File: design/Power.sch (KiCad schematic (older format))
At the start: 49 parts, among them U2 NCP1117ST33T3G, U3 DRV8302

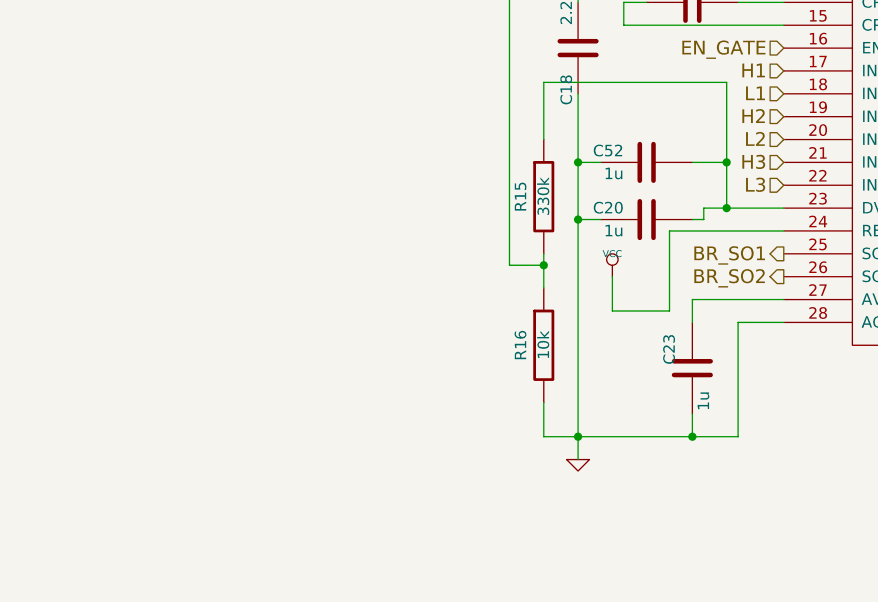
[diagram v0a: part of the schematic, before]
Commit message: Changed some capacitor values, made new assembly PDFs, added comment about R16 to schematic
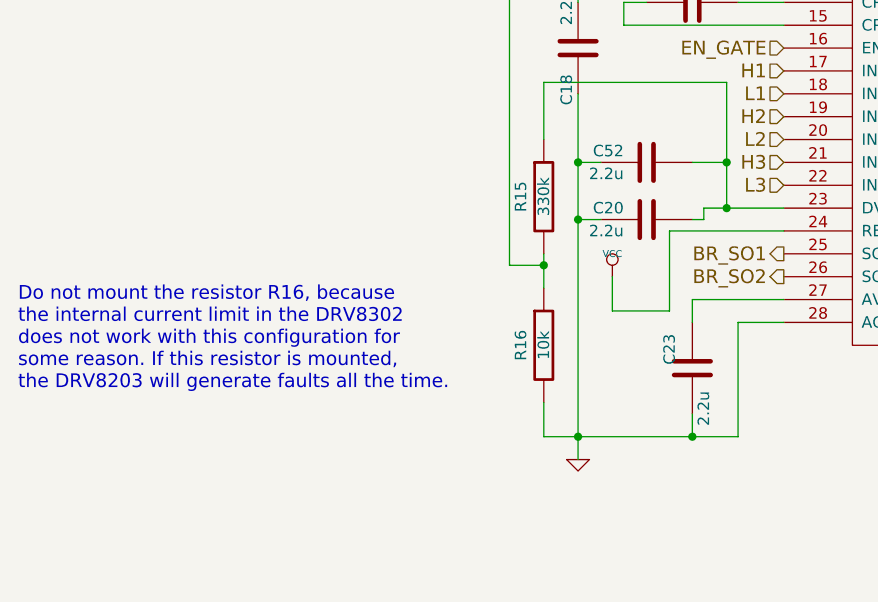
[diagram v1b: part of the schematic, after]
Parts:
- C20, C23, C52: value 1u -> 2.2u
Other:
- note added: "Do not mount the resistor R16, because\nthe internal current limit in the DRV8302\ndoes not work with this configuration for\nsome reason. If this resistor is mounted, \nthe DRV8203 will generate faults all the time."
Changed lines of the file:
@@
 P 3950 4800
 F 0 "C20" V 4000 4900 50  0000 L CNN
-F 1 "1u" V 3900 4900 50  0000 L CNN
+F 1 "2.2u" V 3900 4900 50  0000 L CNN
 F 2 "SMD_Packages:SMD-0603_c" H 3950 4800 60  0001 C CNN
 F 3 "" H 3950 4800 60  0001 C CNN
@@
 P 4150 5450
 F 0 "C23" V 4250 5300 50  0000 L CNN
-F 1 "1u" V 4100 5550 50  0000 L CNN
+F 1 "2.2u" V 4100 5550 50  0000 L CNN
 F 2 "SMD_Packages:SMD-0805" H 4150 5450 60  0001 C CNN
 F 3 "" H 4150 5450 60  0001 C CNN
@@
 P 3950 4550
 F 0 "C52" V 4000 4650 50  0000 L CNN
-F 1 "1u" V 3900 4650 50  0000 L CNN
+F 1 "2.2u" V 3900 4650 50  0000 L CNN
 F 2 "SMD_Packages:SMD-0603_c" H 3950 4550 60  0001 C CNN
 F 3 "" H 3950 4550 60  0001 C CNN
@@
 0D 0D 85 50 5B 08 A1 71 E3 C6 45 47 47 77 AB F8 CD C0 F0 65 C3 18 9A 0F 4F 4B 4B 4B 51 51 51 53
 53 93 40 20 30 31 31 61 94 40 19 18 18 43 C3 C0 C0 A0 72 FE 07 CF 64 8C 61 E1 12 74 DD 00 00 00
-00 49 45 4E 44 AE 42 60 82 CF
+00 49 45 4E 44 AE 42 60 82 05
 EndData
 $EndBitmap
@@
 20 10 88 31 C3 77 F3 62 81 40 20 10 08 04 02 81 E0 1F 14 E4 21 10 08 04 02 81 40 8C 41 50 90 87
 40 20 10 08 04 02 31 06 41 41 1E 02 81 40 20 10 08 C4 18 E4 FF 01 14 B1 03 90 4A B9 68 69 00 00
-00 00 49 45 4E 44 AE 42 60 82 03
+00 00 49 45 4E 44 AE 42 60 82 00
 EndData
 $EndBitmap
@@
 A1 C7 18 00 00 C0 28 C8 B2 00 00 00 46 41 96 05 00 00 30 0A B2 2C 00 00 80 51 90 65 01 00 00 8C
 82 2C 0B 00 00 60 14 64 59 00 00 00 A3 FC 7F BD 9B 69 A6 C1 67 F0 EA 00 00 00 00 49 45 4E 44 AE
-42 60 82 0F
+42 60 82 5F
 EndData
 $EndBitmap
@@
 AB D8 39 0B 59 91 9E DF A8 2A 5B EE 54 3A FD 71 ED 71 2F 29 C3 82 EC 80 87 06 6E C3 98 10 30 3B
 62 9A BB 2D 03 B8 C4 64 FC B5 26 AC 13 9B D1 39 40 41 C1 D6 78 4C 84 BF 94 F0 6F E1 BF 96 F0 0F
-FF 77 E2 FF 1F 0F 43 55 32 21 1C 08 16 00 00 00 00 49 45 4E 44 AE 42 60 82 79
+FF 77 E2 FF 1F 0F 43 55 32 21 1C 08 16 00 00 00 00 49 45 4E 44 AE 42 60 82 4E
 EndData
 $EndBitmap
+Text Notes 1200 5550 0    60   ~ 0
+Do not mount the resistor R16, because\nthe internal current limit in the DRV8302\ndoes not work with this configuration for\nsome reason. If this resistor is mounted, \nthe DRV8203 will generate faults all the time.
 $EndSCHEMATC

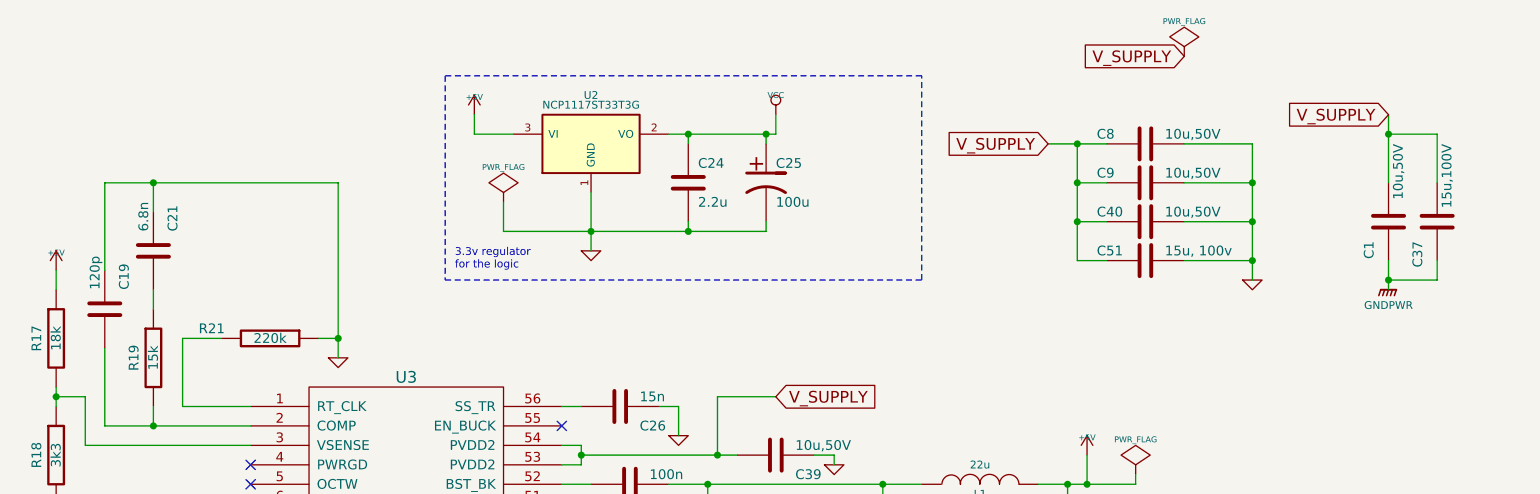
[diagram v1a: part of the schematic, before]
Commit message: Added TVS diode, moved some traces
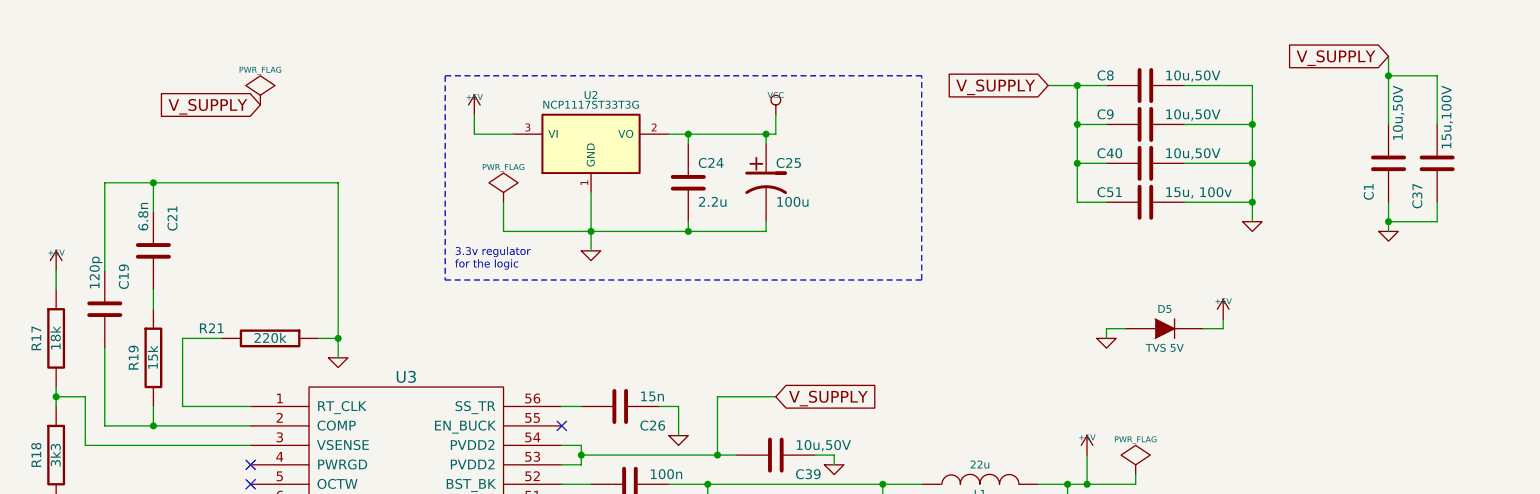
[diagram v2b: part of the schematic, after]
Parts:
- added D5: TVS 5V, w_smd_diode:do214ac, symbol DIODE
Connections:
- net GNDPWR is gone; now on net GND: C1.1, C37.1
- net +5V: now also D5.2 (K)
- net GND: now also D5.1 (A)
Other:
- moved on the sheet: C1, C37, C40, C51, C8, C9
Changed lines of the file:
@@
 LIBS:crf_1
 LIBS:BLDC_4-cache
-EELAYER 25 0
+EELAYER 24 0
 EELAYER END
 $Descr A4 11693 8268
@@
 L PWR_FLAG #FLG066
 U 1 1 505105A5
-P 9350 750
-F 0 "#FLG066" H 9350 845 30  0001 C CNN
-F 1 "PWR_FLAG" H 9350 930 30  0000 C CNN
-F 2 "" H 9350 750 60  0001 C CNN
-F 3 "" H 9350 750 60  0001 C CNN
-	1    9350 750
+P 4600 1000
+F 0 "#FLG066" H 4600 1095 30  0001 C CNN
+F 1 "PWR_FLAG" H 4600 1180 30  0000 C CNN
+F 2 "" H 4600 1000 60  0001 C CNN
+F 3 "" H 4600 1000 60  0001 C CNN
+	1    4600 1000
 	1    0    0    -1
 $EndComp
@@
 L C C51
 U 1 1 51094370
-P 9150 1800
-F 0 "C51" V 9100 1550 50  0000 L CNN
-F 1 "15u, 100v" V 9100 1900 50  0000 L CNN
-F 2 "w_smd_cap:c_2220" H 9150 1800 60  0001 C CNN
-F 3 "" H 9150 1800 60  0001 C CNN
-	1    9150 1800
+P 9150 1500
+F 0 "C51" V 9100 1250 50  0000 L CNN
+F 1 "15u, 100v" V 9100 1600 50  0000 L CNN
+F 2 "w_smd_cap:c_2220" H 9150 1500 60  0001 C CNN
+F 3 "" H 9150 1500 60  0001 C CNN
+	1    9150 1500
 	0    1    1    0
 $EndComp
@@
 L GND #PWR069
 U 1 1 510944D0
-P 9700 1900
-F 0 "#PWR069" H 9700 1900 30  0001 C CNN
-F 1 "GND" H 9700 1830 30  0001 C CNN
-F 2 "" H 9700 1900 60  0001 C CNN
-F 3 "" H 9700 1900 60  0001 C CNN
-	1    9700 1900
+P 9700 1600
+F 0 "#PWR069" H 9700 1600 30  0001 C CNN
+F 1 "GND" H 9700 1530 30  0001 C CNN
+F 2 "" H 9700 1600 60  0001 C CNN
+F 3 "" H 9700 1600 60  0001 C CNN
+	1    9700 1600
 	1    0    0    -1
 $EndComp
@@
 L C C1
 U 1 1 523435A0
-P 10400 1600
-F 0 "C1" V 10500 1700 50  0000 L CNN
-F 1 "10u,50V" V 10350 1200 50  0000 L CNN
-F 2 "SMD_Packages:SMD-1206" H 10400 1600 60  0001 C CNN
-F 3 "" H 10400 1600 60  0001 C CNN
-	1    10400 1600
+P 10400 1300
+F 0 "C1" V 10500 1400 50  0000 L CNN
+F 1 "10u,50V" V 10350 900 50  0000 L CNN
+F 2 "SMD_Packages:SMD-1206" H 10400 1300 60  0001 C CNN
+F 3 "" H 10400 1300 60  0001 C CNN
+	1    10400 1300
 	-1   0    0    1
 $EndComp
@@
 L C C37
 U 1 1 523435AB
-P 10650 1600
-F 0 "C37" V 10750 1700 50  0000 L CNN
-F 1 "15u,100V" V 10600 1200 50  0000 L CNN
-F 2 "w_smd_cap:c_2220" H 10650 1600 60  0001 C CNN
-F 3 "" H 10650 1600 60  0001 C CNN
-	1    10650 1600
+P 10650 1300
+F 0 "C37" V 10750 1400 50  0000 L CNN
+F 1 "15u,100V" V 10600 900 50  0000 L CNN
+F 2 "w_smd_cap:c_2220" H 10650 1300 60  0001 C CNN
+F 3 "" H 10650 1300 60  0001 C CNN
+	1    10650 1300
 	-1   0    0    1
 $EndComp
@@
 	1    0    0    -1
 $EndComp
-Text GLabel 10400 1050 0    60   Input ~ 0
+Text GLabel 10400 750  0    60   Input ~ 0
 V_SUPPLY
-Text GLabel 9350 750  0    60   Input ~ 0
+Text GLabel 4600 1000 0    60   Input ~ 0
 V_SUPPLY
-Text GLabel 8650 1200 0    60   Input ~ 0
+Text GLabel 8650 900  0    60   Input ~ 0
 V_SUPPLY
 $Comp
 L C C40
 U 1 1 53E7AF97
-P 9150 1600
-F 0 "C40" V 9100 1350 50  0000 L CNN
-F 1 "10u,50V" V 9100 1700 50  0000 L CNN
-F 2 "SMD_Packages:SMD-1206" H 9150 1600 60  0001 C CNN
-F 3 "" H 9150 1600 60  0001 C CNN
-	1    9150 1600
+P 9150 1300
+F 0 "C40" V 9100 1050 50  0000 L CNN
+F 1 "10u,50V" V 9100 1400 50  0000 L CNN
+F 2 "SMD_Packages:SMD-1206" H 9150 1300 60  0001 C CNN
+F 3 "" H 9150 1300 60  0001 C CNN
+	1    9150 1300
 	0    1    1    0
 $EndComp
@@
 L C C9
 U 1 1 53E7AFA2
-P 9150 1400
-F 0 "C9" V 9100 1150 50  0000 L CNN
-F 1 "10u,50V" V 9100 1500 50  0000 L CNN
-F 2 "SMD_Packages:SMD-1206" H 9150 1400 60  0001 C CNN
-F 3 "" H 9150 1400 60  0001 C CNN
-	1    9150 1400
+P 9150 1100
+F 0 "C9" V 9100 850 50  0000 L CNN
+F 1 "10u,50V" V 9100 1200 50  0000 L CNN
+F 2 "SMD_Packages:SMD-1206" H 9150 1100 60  0001 C CNN
+F 3 "" H 9150 1100 60  0001 C CNN
+	1    9150 1100
 	0    1    1    0
 $EndComp
@@
 L C C8
 U 1 1 53E7AFAD
-P 9150 1200
-F 0 "C8" V 9100 950 50  0000 L CNN
-F 1 "10u,50V" V 9100 1300 50  0000 L CNN
-F 2 "SMD_Packages:SMD-1206" H 9150 1200 60  0001 C CNN
-F 3 "" H 9150 1200 60  0001 C CNN
-	1    9150 1200
+P 9150 900
+F 0 "C8" V 9100 650 50  0000 L CNN
+F 1 "10u,50V" V 9100 1000 50  0000 L CNN
+F 2 "SMD_Packages:SMD-1206" H 9150 900 60  0001 C CNN
+F 3 "" H 9150 900 60  0001 C CNN
+	1    9150 900
 	0    1    1    0
 $EndComp
@@
 Text HLabel 7600 5150 2    60   Input ~ 0
 SH2_B
-$Comp
-L GNDPWR #PWR070
-U 1 1 53FA36C6
-P 10400 1950
-F 0 "#PWR070" H 10400 2000 40  0001 C CNN
-F 1 "GNDPWR" H 10400 1870 40  0000 C CNN
-F 2 "" H 10400 1950 60  0000 C CNN
-F 3 "" H 10400 1950 60  0000 C CNN
-	1    10400 1950
-	1    0    0    -1
-$EndComp
 Text HLabel 10600 3350 2    60   Input ~ 0
 H3_VS
@@
 	6300 6500 6100 6500
 Wire Wire Line
-	9700 1800 9350 1800
+	9700 1500 9350 1500
 Wire Wire Line
-	9700 1200 9700 1900
+	9700 900  9700 1600
 Wire Wire Line
 	3750 4550 3650 4550
@@
 Connection ~ 3750 3250
 Wire Wire Line
-	10400 1050 10400 1400
+	10400 750  10400 1100
 Wire Wire Line
-	10650 1150 10650 1400
-Connection ~ 10400 1150
+	10650 850  10650 1100
+Connection ~ 10400 850
 Wire Wire Line
-	10400 1800 10400 1950
+	10400 1500 10400 1650
 Wire Wire Line
-	10650 1900 10650 1800
-Connection ~ 10400 1900
+	10650 1600 10650 1500
+Connection ~ 10400 1600
 Wire Wire Line
-	10400 1900 10650 1900
+	10400 1600 10650 1600
 Wire Wire Line
-	10400 1150 10650 1150
+	10400 850  10650 850
 Wire Wire Line
 	4150 4800 4200 4800
@@
 Connection ~ 4300 4750
 Wire Wire Line
-	8650 1200 8950 1200
+	8650 900  8950 900
 Wire Wire Line
-	8800 1200 8800 1800
+	8800 900  8800 1500
 Wire Wire Line
-	8800 1800 8950 1800
-Connection ~ 8800 1200
+	8800 1500 8950 1500
+Connection ~ 8800 900
 Wire Wire Line
-	8950 1600 8800 1600
-Connection ~ 8800 1600
+	8950 1300 8800 1300
+Connection ~ 8800 1300
 Wire Wire Line
-	8950 1400 8800 1400
-Connection ~ 8800 1400
+	8950 1100 8800 1100
+Connection ~ 8800 1100
 Wire Wire Line
-	9350 1200 9700 1200
-Connection ~ 9700 1800
+	9350 900  9700 900
+Connection ~ 9700 1500
 Wire Wire Line
-	9350 1400 9700 1400
-Connection ~ 9700 1400
+	9350 1100 9700 1100
+Connection ~ 9700 1100
 Wire Wire Line
-	9350 1600 9700 1600
-Connection ~ 9700 1600
+	9350 1300 9700 1300
+Connection ~ 9700 1300
 $Bitmap
 Pos 1800 2050
@@
 0D 0D 85 50 5B 08 A1 71 E3 C6 45 47 47 77 AB F8 CD C0 F0 65 C3 18 9A 0F 4F 4B 4B 4B 51 51 51 53
 53 93 40 20 30 31 31 61 94 40 19 18 18 43 C3 C0 C0 A0 72 FE 07 CF 64 8C 61 E1 12 74 DD 00 00 00
-00 49 45 4E 44 AE 42 60 82 05
+00 49 45 4E 44 AE 42 60 82 01
 EndData
 $EndBitmap
@@
 A1 C7 18 00 00 C0 28 C8 B2 00 00 00 46 41 96 05 00 00 30 0A B2 2C 00 00 80 51 90 65 01 00 00 8C
 82 2C 0B 00 00 60 14 64 59 00 00 00 A3 FC 7F BD 9B 69 A6 C1 67 F0 EA 00 00 00 00 49 45 4E 44 AE
-42 60 82 5F
+42 60 82 00
 EndData
 $EndBitmap
@@
 AB D8 39 0B 59 91 9E DF A8 2A 5B EE 54 3A FD 71 ED 71 2F 29 C3 82 EC 80 87 06 6E C3 98 10 30 3B
 62 9A BB 2D 03 B8 C4 64 FC B5 26 AC 13 9B D1 39 40 41 C1 D6 78 4C 84 BF 94 F0 6F E1 BF 96 F0 0F
-FF 77 E2 FF 1F 0F 43 55 32 21 1C 08 16 00 00 00 00 49 45 4E 44 AE 42 60 82 4E
+FF 77 E2 FF 1F 0F 43 55 32 21 1C 08 16 00 00 00 00 49 45 4E 44 AE 42 60 82 1A
 EndData
 $EndBitmap
 Text Notes 1200 5550 0    60   ~ 0
 Do not mount the resistor R16, because\nthe internal current limit in the DRV8302\ndoes not work with this configuration for\nsome reason. If this resistor is mounted, \nthe DRV8203 will generate faults all the time.
+$Comp
+L DIODE D5
+U 1 1 548EDCBC
+P 9250 2150
+F 0 "D5" H 9250 2250 40  0000 C CNN
+F 1 "TVS 5V" H 9250 2050 40  0000 C CNN
+F 2 "w_smd_diode:do214ac" H 9250 2150 60  0001 C CNN
+F 3 "" H 9250 2150 60  0000 C CNN
+	1    9250 2150
+	1    0    0    -1
+$EndComp
+$Comp
+L +5V #PWR070
+U 1 1 548EDECA
+P 9550 2100
+F 0 "#PWR070" H 9550 2190 20  0001 C CNN
+F 1 "+5V" H 9550 2190 30  0000 C CNN
+F 2 "" H 9550 2100 60  0001 C CNN
+F 3 "" H 9550 2100 60  0001 C CNN
+	1    9550 2100
+	1    0    0    -1
+$EndComp
+$Comp
+L GND #PWR071
+U 1 1 548EDF07
+P 8950 2200
+F 0 "#PWR071" H 8950 2200 30  0001 C CNN
+F 1 "GND" H 8950 2130 30  0001 C CNN
+F 2 "" H 8950 2200 60  0001 C CNN
+F 3 "" H 8950 2200 60  0001 C CNN
+	1    8950 2200
+	1    0    0    -1
+$EndComp
+Wire Wire Line
+	8950 2200 8950 2150
+Wire Wire Line
+	8950 2150 9050 2150
+Wire Wire Line
+	9450 2150 9550 2150
+Wire Wire Line
+	9550 2150 9550 2100
+$Comp
+L GND #PWR072
+U 1 1 548F3DC0
+P 10400 1650
+F 0 "#PWR072" H 10400 1650 30  0001 C CNN
+F 1 "GND" H 10400 1580 30  0001 C CNN
+F 2 "" H 10400 1650 60  0001 C CNN
+F 3 "" H 10400 1650 60  0001 C CNN
+	1    10400 1650
+	1    0    0    -1
+$EndComp
 $EndSCHEMATC

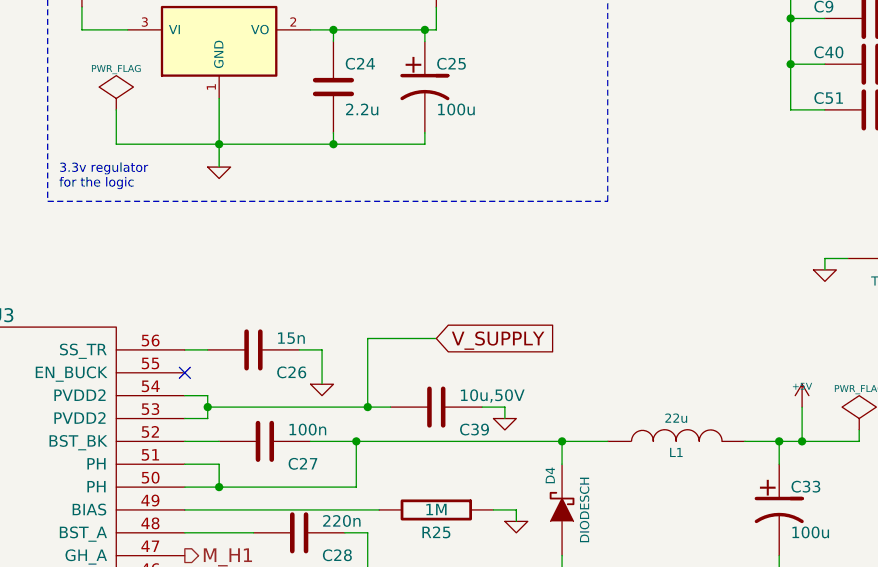
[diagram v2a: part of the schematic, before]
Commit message: Made C26 a do-not-mount cap
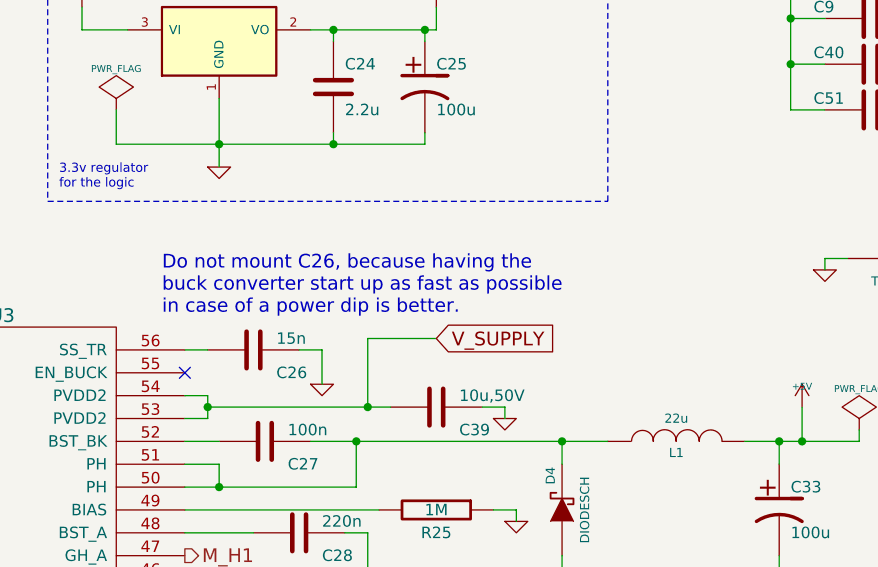
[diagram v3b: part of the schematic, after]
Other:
- note added: "Do not mount C26, because having the\nbuck converter start up as fast as possible\nin case of a power dip is better."
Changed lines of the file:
@@
 LIBS:crf_1
 LIBS:BLDC_4-cache
-EELAYER 24 0
+EELAYER 25 0
 EELAYER END
 $Descr A4 11693 8268
@@
 0D 0D 85 50 5B 08 A1 71 E3 C6 45 47 47 77 AB F8 CD C0 F0 65 C3 18 9A 0F 4F 4B 4B 4B 51 51 51 53
 53 93 40 20 30 31 31 61 94 40 19 18 18 43 C3 C0 C0 A0 72 FE 07 CF 64 8C 61 E1 12 74 DD 00 00 00
-00 49 45 4E 44 AE 42 60 82 01
+00 49 45 4E 44 AE 42 60 82 05
 EndData
 $EndBitmap
@@
 AB D8 39 0B 59 91 9E DF A8 2A 5B EE 54 3A FD 71 ED 71 2F 29 C3 82 EC 80 87 06 6E C3 98 10 30 3B
 62 9A BB 2D 03 B8 C4 64 FC B5 26 AC 13 9B D1 39 40 41 C1 D6 78 4C 84 BF 94 F0 6F E1 BF 96 F0 0F
-FF 77 E2 FF 1F 0F 43 55 32 21 1C 08 16 00 00 00 00 49 45 4E 44 AE 42 60 82 1A
+FF 77 E2 FF 1F 0F 43 55 32 21 1C 08 16 00 00 00 00 49 45 4E 44 AE 42 60 82 27
 EndData
 $EndBitmap
@@
 	1    0    0    -1
 $EndComp
+Text Notes 6050 2400 0    60   ~ 0
+Do not mount C26, because having the\nbuck converter start up as fast as possible\nin case of a power dip is better.
 $EndSCHEMATC
